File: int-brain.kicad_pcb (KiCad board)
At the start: 2 copper layers, 107 x 79.5 mm, 112 parts, among them J1 Top, J10 2MB, J11 1MB, J12 1MA, J13 1MA_ENC, J14 1MB_ENC, J15 2MA_ENC, J16 MPU9250, J17 VBATT_SELECT, J2 Bottom, J3 PWR, J4 PWR, J5 USB_A, J6 2MB_ENC, J7 I2C0, J8 UART0, J9 2MA, SW1 SW_Push, U1 PCA9635, U10 TPS5450DDA, U11 DRV8251ADDAR, U12 INA139, U13 AMS1117-3.3, U2 ESP32-DevKitC, U3 DRV8251ADDAR, U4 INA139, U5 DRV8251ADDAR, U6 INA139, U7 TPS5450DDA, U8 DRV8251ADDAR, U9 INA139

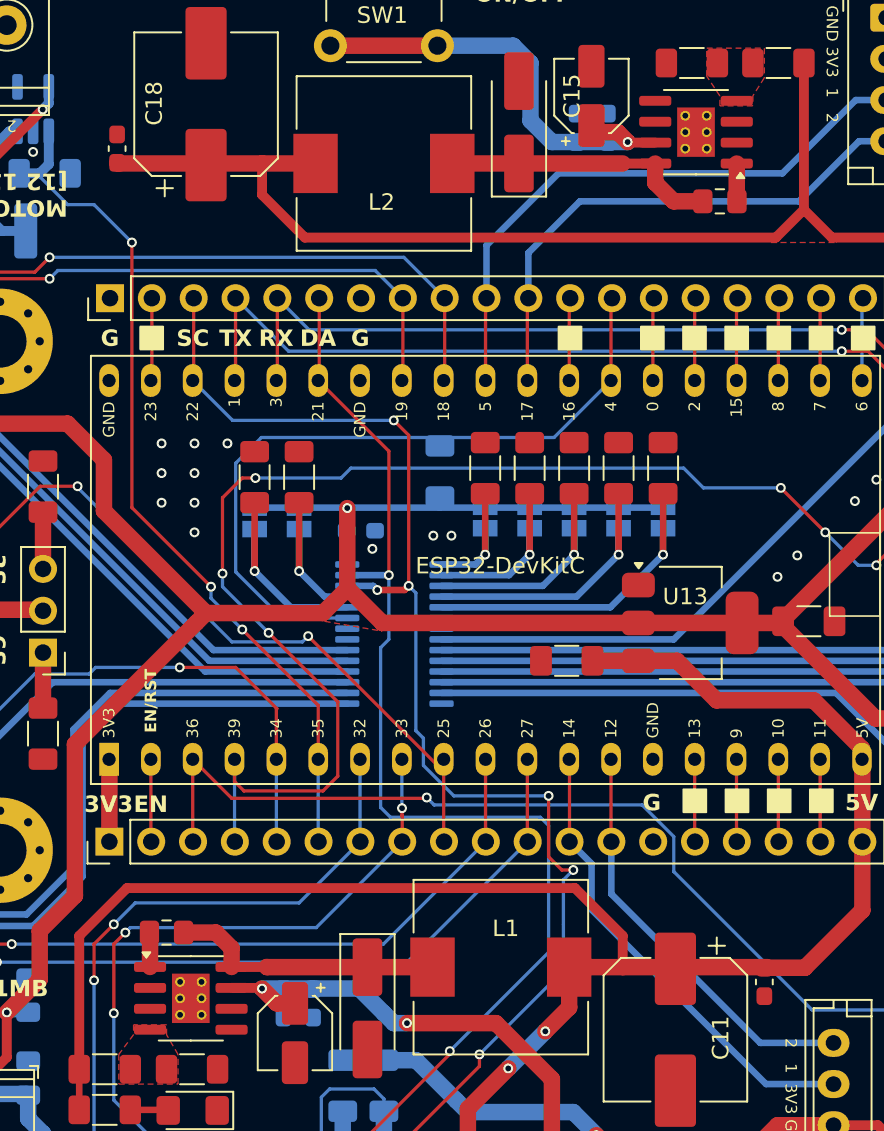
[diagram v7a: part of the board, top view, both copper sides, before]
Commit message: footprint updates
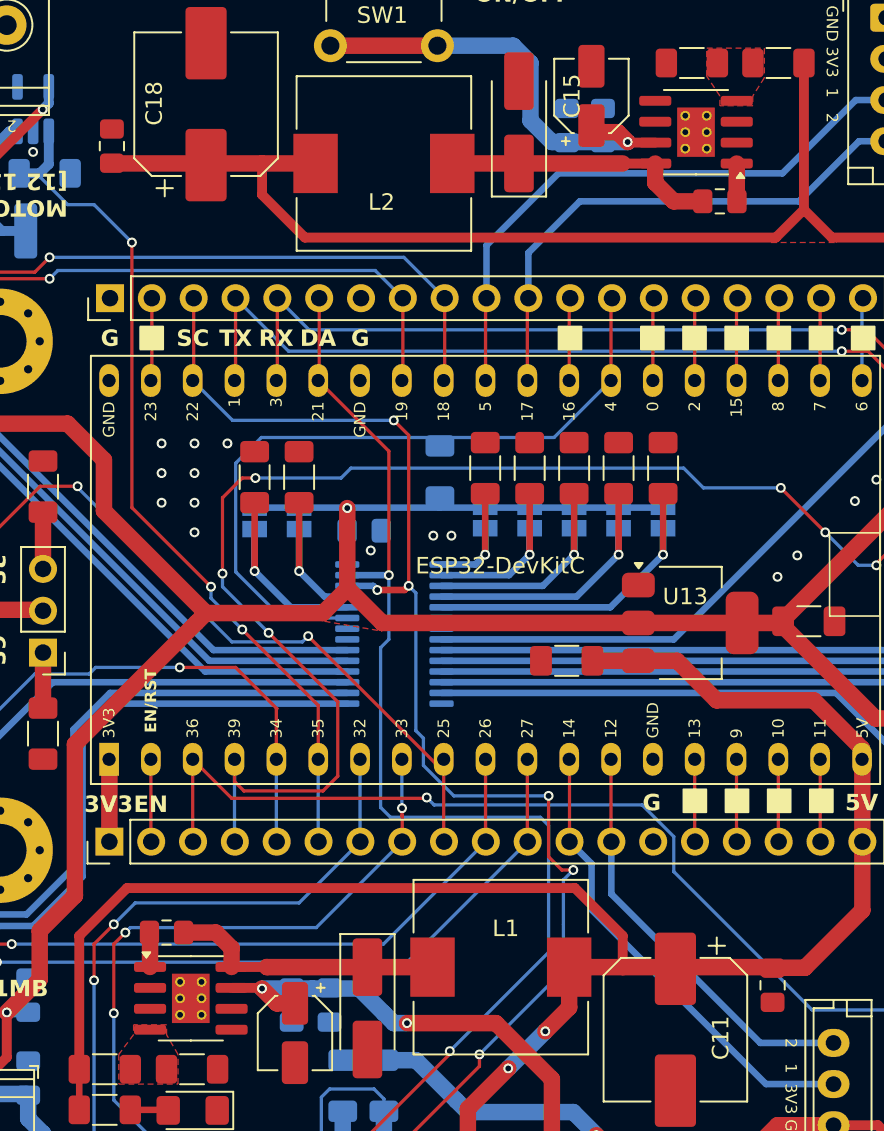
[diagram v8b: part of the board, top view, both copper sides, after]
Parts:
- C1, C16, C22, C23, C24, C25, C9: footprint Capacitor_SMD:C_0603_1608Metric_Pad1.08x0.95mm_HandSolder -> Capacitor_SMD:C_0805_2012Metric_Pad1.18x1.45mm_HandSolder
- D10, D5: value D -> M7
- moved C9 1.00 mm to (80.7, 132.5)
- moved C16 0.62 mm to (95.1, 79.1)
- moved C24 0.54 mm to (107.6, 131.3)
- moved C22 0.51 mm to (78.4, 132.5)
- moved C25 0.35 mm to (67.5, 80.3)
- moved C23 0.33 mm to (97.3, 79.1)
- moved C1 0.20 mm to (82.8, 103.7)
